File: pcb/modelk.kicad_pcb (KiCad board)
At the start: 2 copper layers, 150 x 38 mm, 50 parts, among them J1 JST-PH connector, J2 Conn_01x20, J3 Conn_01x05, J4 Conn_01x12, J5 Conn_01x04, J6 Conn_01x08, J7 Faston PCB mount, SW1 SW_reset, U1 nice_nano, U2 74HC595, U3 74HC595, U4 74HC595

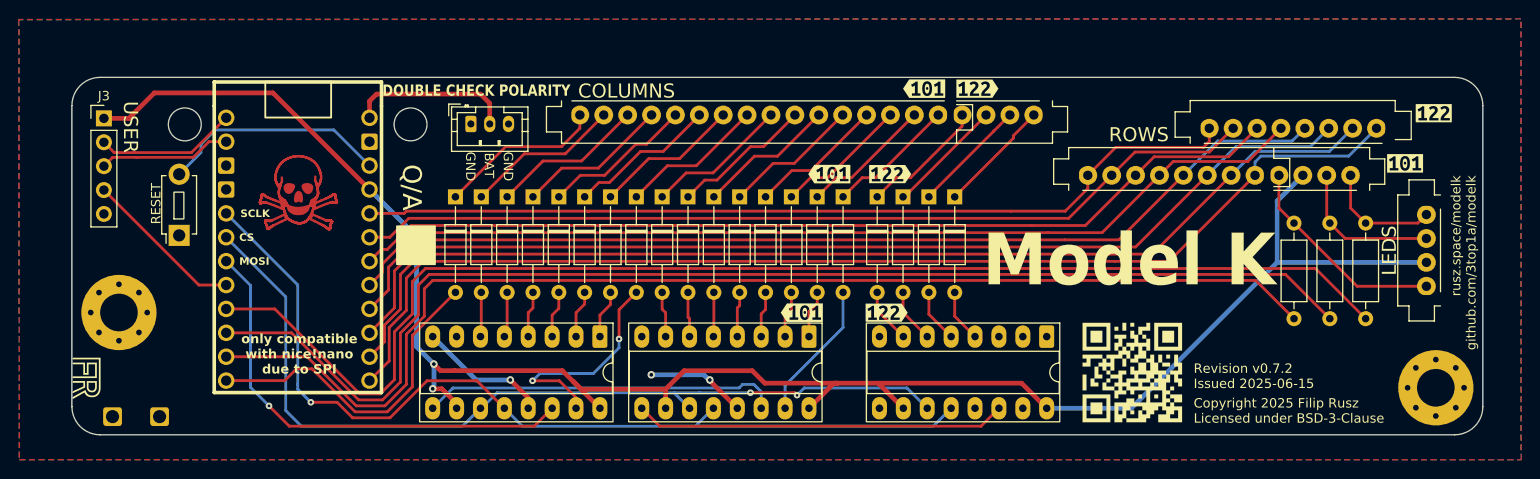
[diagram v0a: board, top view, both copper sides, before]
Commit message: Added battery header for profiling
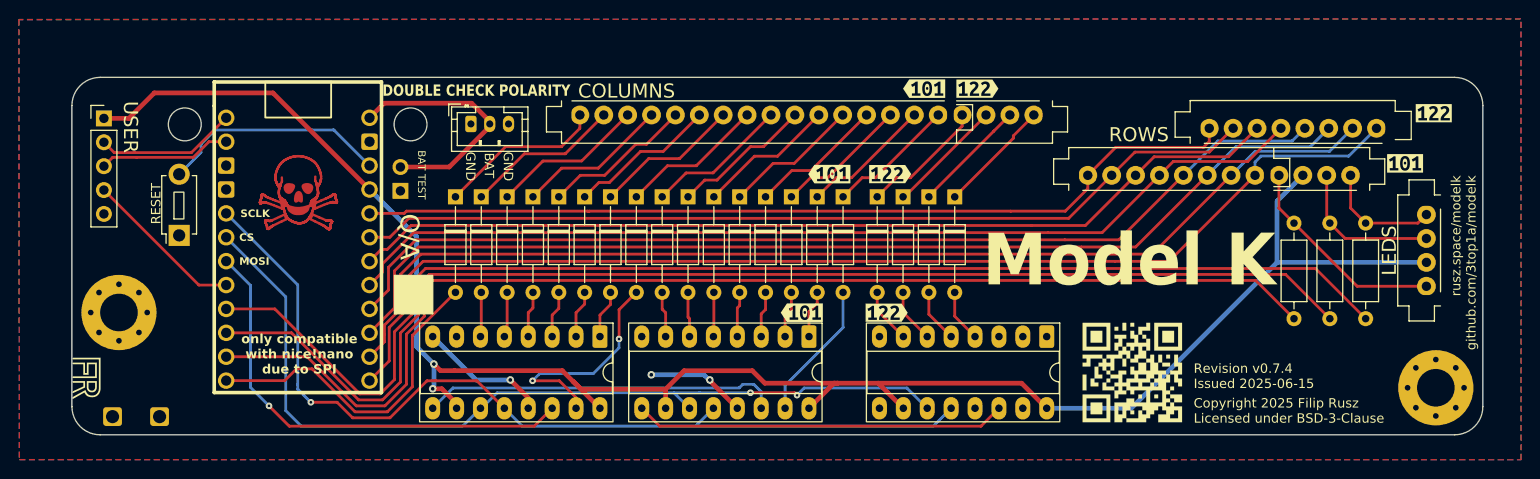
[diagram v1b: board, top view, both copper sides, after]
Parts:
- added J8: Dupont for power profiling, Library:BatteryHeader, F.Cu at (99.7, 59.1)
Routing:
- net +BATT: track 17.5 -> 26.0 mm
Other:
- board text added: "BAT TEST"
- board text added: "TODO: Decluter Move diodes closer to connector Reroute? Better visual design Better font Design language"
- board text removed: "TODO:"

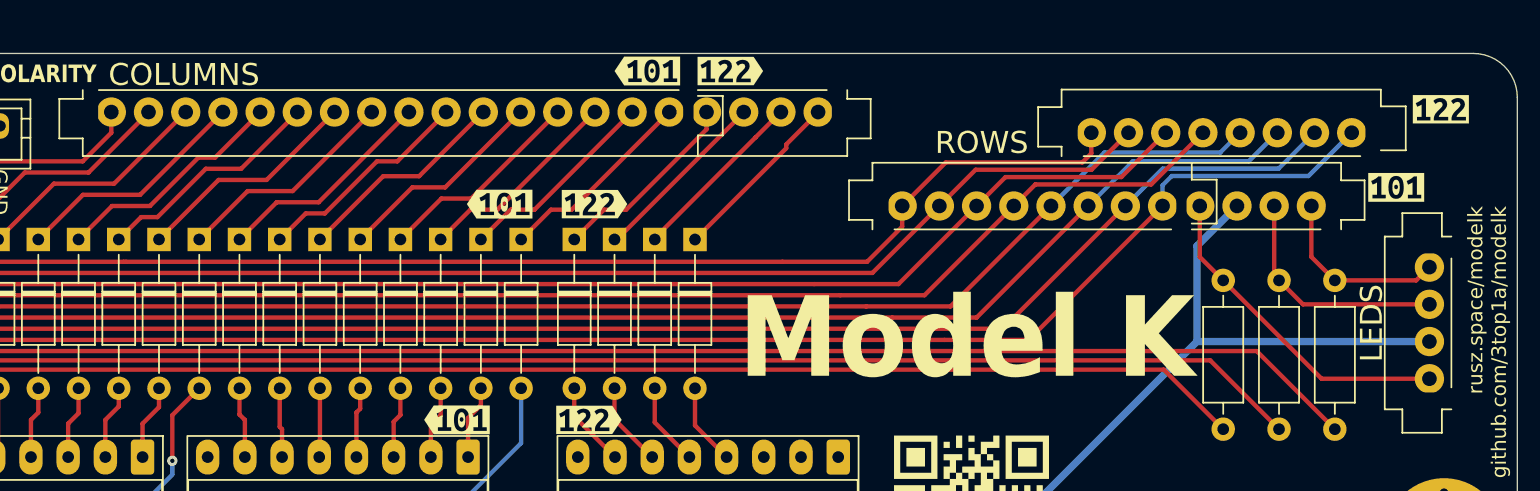
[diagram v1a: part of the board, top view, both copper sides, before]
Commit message: Removed mount holes from ffc connectors
This also fixes all DRC errors.
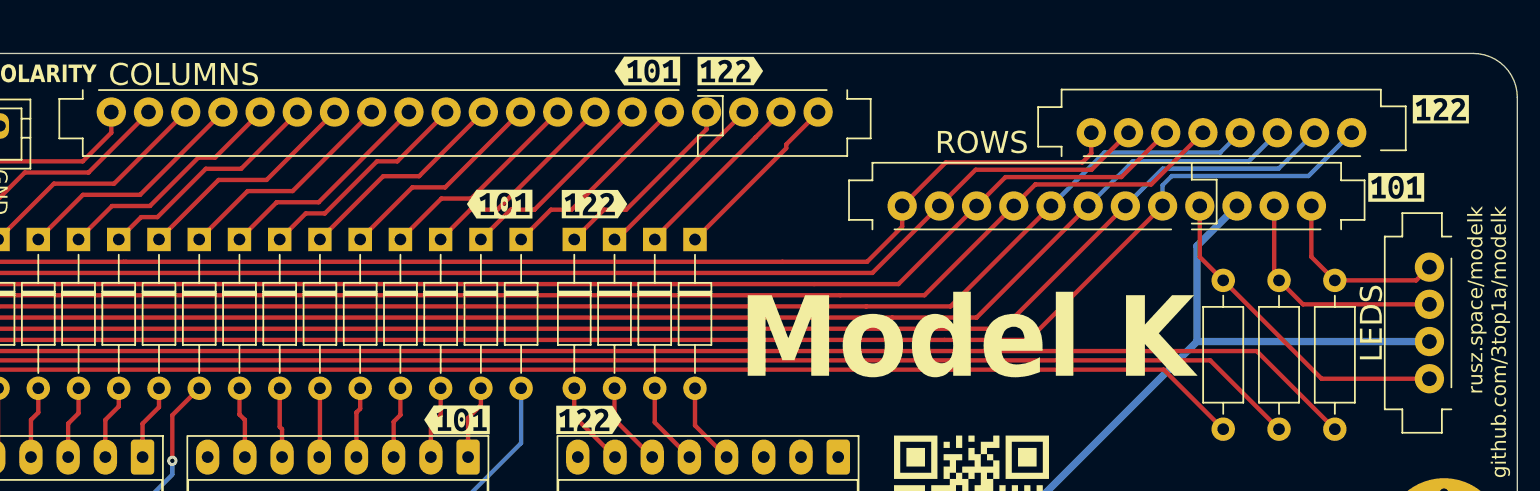
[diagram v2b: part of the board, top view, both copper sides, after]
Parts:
- J2: footprint Library:ModelH-triomate-cols20 -> Library:ffc-cols20
- J3: value Conn_01x05 -> User exposed
- J4: footprint Library:ModelH-triomate-rows12 -> Library:ffc-rows12
- J5: footprint Library:ModelH-triomate-leds4 -> Library:ffc-leds4
- J6: footprint Library:ModelH-triomate-rows8 -> Library:ffc-rows8

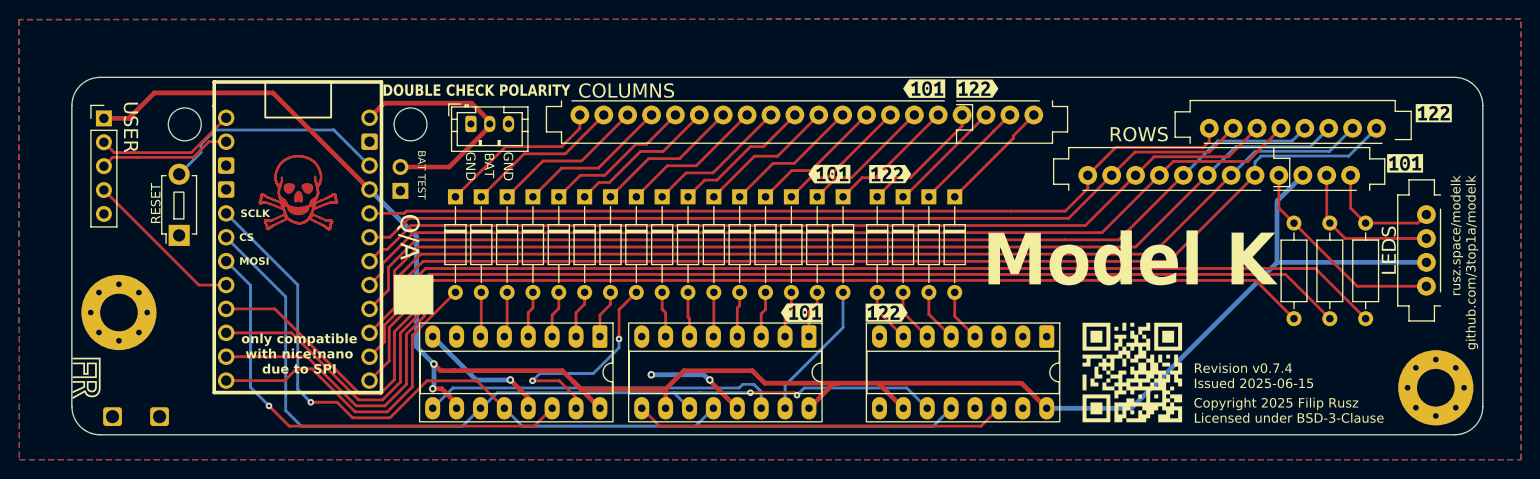
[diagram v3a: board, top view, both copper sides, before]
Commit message: All leds on high frequency pins
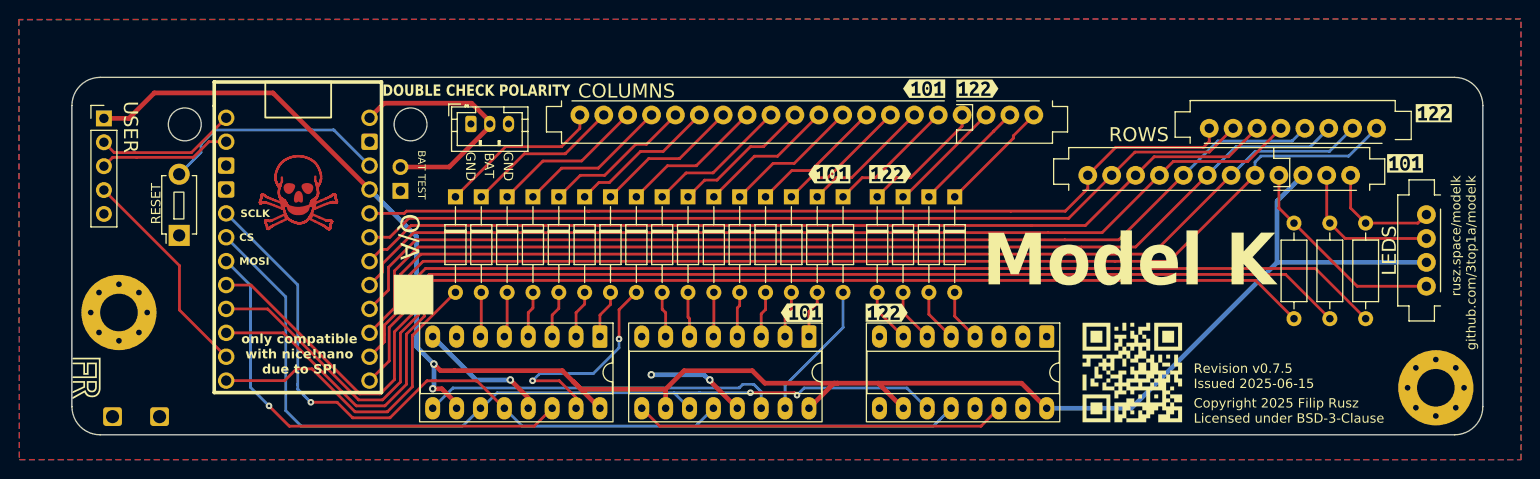
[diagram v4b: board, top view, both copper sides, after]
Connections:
- U1 pad 10: led2 -> led1
- U1 pad 11: led1 -> led0
- U1 pad 12: led0 -> user3
- U1 pad 9: user3 -> led2
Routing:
- net user3: track 17.2 -> 23.1 mm
- net led1: track 132.7 -> 133.7 mm
- net led0: track 127.7 -> 128.8 mm
- net led2: track 137.6 -> 138.7 mm

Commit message: Remade half the board
Redid the visual language, standardized the font and its size.
Moved diodes closer to connector.
Text is all caps now.
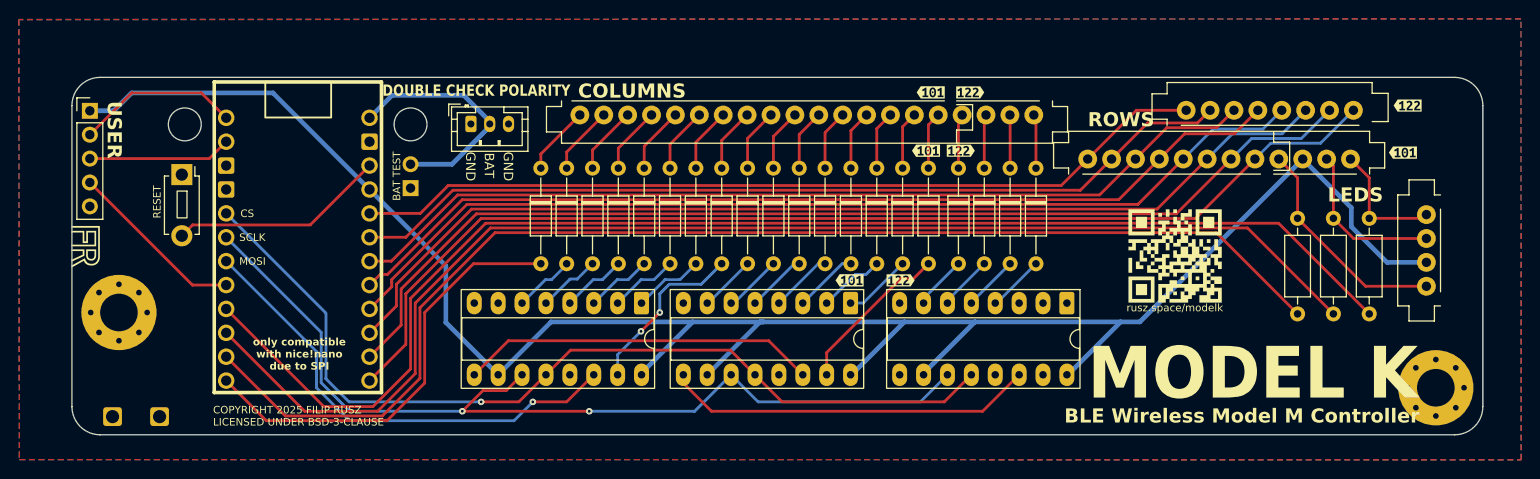
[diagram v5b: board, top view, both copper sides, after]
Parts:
- removed the G*** at (144.2, 44.9)
- removed REF**: Symbol_Danger_8x8mm_Copper, Symbol:Symbol_Danger_8x8mm_Copper
- removed kibuzzard-6839B796 (x3): G***, kibuzzard-6839B796
- removed kibuzzard-684051F2: G***, kibuzzard-684051F2
- removed kibuzzard-684051F7: G***, kibuzzard-684051F7
- removed kibuzzard-684051FA: G***, kibuzzard-684051FA
- removed kibuzzard-684DE304: G***, kibuzzard-684DE304
- removed kibuzzard-684DE317: G***, kibuzzard-684DE317
- added G***: LOGO, Library:LOGO-QR, F.Cu at (182.3, 66.0)
- added kibuzzard-684FF45F: G***, kibuzzard-684FF45F, F.Cu at (147.4, 68.6)
- added kibuzzard-684FF45F: G***, kibuzzard-684FF45F, F.Cu at (156.1, 48.6)
- added kibuzzard-684FF45F: G***, kibuzzard-684FF45F, F.Cu at (155.6, 54.8)
- added kibuzzard-684FF45F: G***, kibuzzard-684FF45F, F.Cu at (206.3, 55.0)
- added kibuzzard-684FF466: G***, kibuzzard-684FF466, F.Cu at (160.3, 48.6)
- added kibuzzard-684FF466: G***, kibuzzard-684FF466, F.Cu at (152.9, 68.6)
- added kibuzzard-684FF466: G***, kibuzzard-684FF466, F.Cu at (159.3, 54.8)
- added kibuzzard-684FF5A3: G***, kibuzzard-684FF5A3, F.Cu at (206.8, 50.0)
- moved G*** 14.0 mm to (64.4, 65.8)
- moved D10 9.58 mm to (139.3, 56.6)
- moved D14 9.58 mm to (150.3, 56.6)
- moved D15 9.58 mm to (153.1, 56.6)
- moved D9 9.58 mm to (136.6, 56.6)
- moved D1 9.58 mm to (114.6, 56.6)
- moved D3 9.58 mm to (120.1, 56.6)
- moved D4 9.58 mm to (122.9, 56.6)
- moved D5 9.58 mm to (125.6, 56.6)
- moved D6 9.58 mm to (128.4, 56.6)
- moved D11 9.58 mm to (142.1, 56.6)
- moved D12 9.58 mm to (144.8, 56.6)
- moved D13 9.58 mm to (147.6, 56.6)
- moved D16 9.58 mm to (155.8, 56.6)
- moved D2 9.58 mm to (117.4, 56.6)
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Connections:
- U1 pad 10: led1 -> led2
- U1 pad 11: led0 -> led1
- U1 pad 12: user3 -> led0
- U1 pad 9: led2 -> user3
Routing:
- net GND: track 24.6 -> 0.00 mm, vias 3 -> 0
- net +3.3V: track 201.3 -> 214.2 mm, vias 2 -> 0
- net col0: track 35.2 -> 46.5 mm
- net Net-(D1-K): track 17.7 -> 7.37 mm
- net Net-(D2-K): track 16.6 -> 7.28 mm
- net Net-(D3-K): track 16.4 -> 7.20 mm
- net Net-(D4-K): track 16.2 -> 7.11 mm
- net Net-(D5-K): track 16.0 -> 7.03 mm
- net Net-(D6-K): track 15.9 -> 6.94 mm
- net Net-(D7-K): track 15.6 -> 6.86 mm
- net Net-(D8-K): track 15.4 -> 6.77 mm
- net Net-(D9-K): track 15.2 -> 6.68 mm
- net Net-(D10-K): track 15.0 -> 6.60 mm
- net Net-(D11-K): track 14.8 -> 6.51 mm
- net Net-(D12-K): track 14.6 -> 6.43 mm
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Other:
- board text added: "BLE Wireless Model M Controller"
- board text added: "COPYRIGHT 2025 FILIP RUSZ LICENSED UNDER BSD-3-CLAUSE"
- board text added: "MODEL K"
- board text added: "REVISION ${REVISION} ISSUED ${ISSUE_DATE}"
- board text added: "TODO: Better font?"
- board text added: "rusz.space/modelk"
- board text removed: "Copyright 2025 Filip Rusz Licensed under BSD-3-Clause"
- board text removed: "Revision ${REVISION} Issued ${ISSUE_DATE}"
- board text removed: "TODO: Decluter Move diodes closer to connector Reroute? Better visual design Better font Design language"
- board text removed: "rusz.space/modelk github.com/3top1a/modelk"

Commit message: Better font
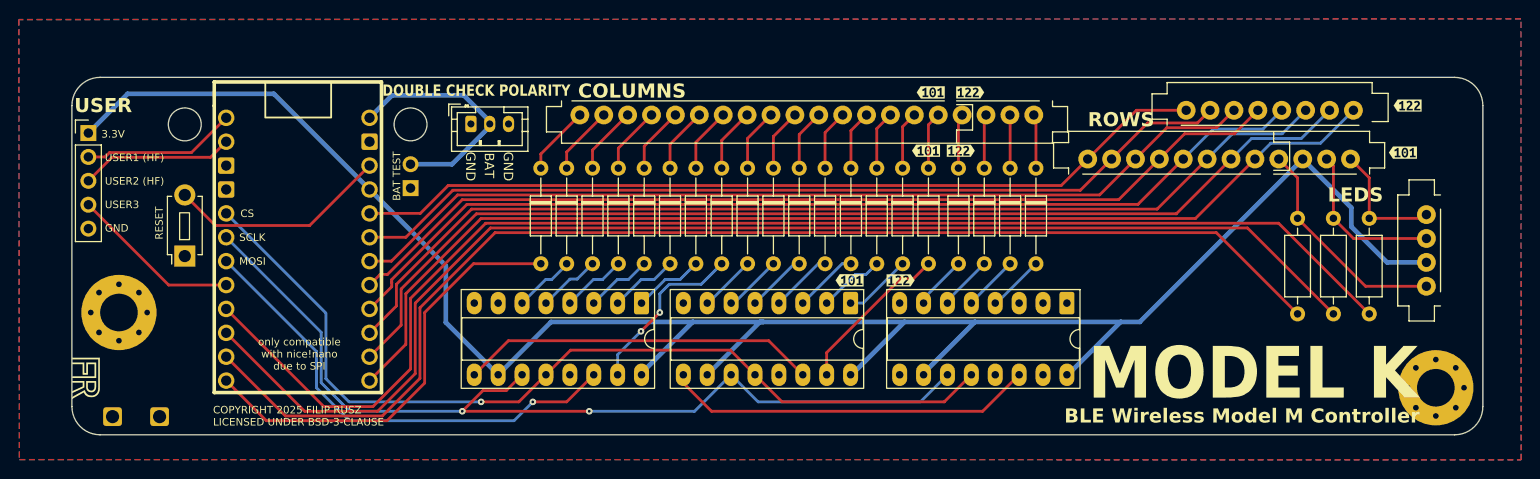
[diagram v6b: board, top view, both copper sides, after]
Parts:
- G***: moved to B.Cu
- moved G*** 74.7 mm to (107.6, 63.0), turned to 180 degrees
- moved G*** 14.0 mm to (64.4, 79.8)
- moved SW1 8.67 mm to (76.8, 66.0), turned to 90 degrees
- moved J3 2.37 mm to (66.5, 52.9)
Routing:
- net user1: track 17.4 -> 16.1 mm
- net user2: track 15.2 -> 16.4 mm
- net +3.3V: track 214.2 -> 215.0 mm
- net user3: track 19.0 -> 18.2 mm
- net Net-(U1-RST): track 23.0 -> 23.6 mm
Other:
- board text added: "3.3V"
- board text added: "USER1 (HF)"
- board text added: "USER2 (HF)"
- board text added: "USER3"
